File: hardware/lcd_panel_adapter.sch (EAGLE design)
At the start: 50 parts, among them IC1 TPS65131RGET, IC2 LP8867CQPWPRQ1, J1 245863050104829+, J2 54548-2271, U1 TLV62080DSGR

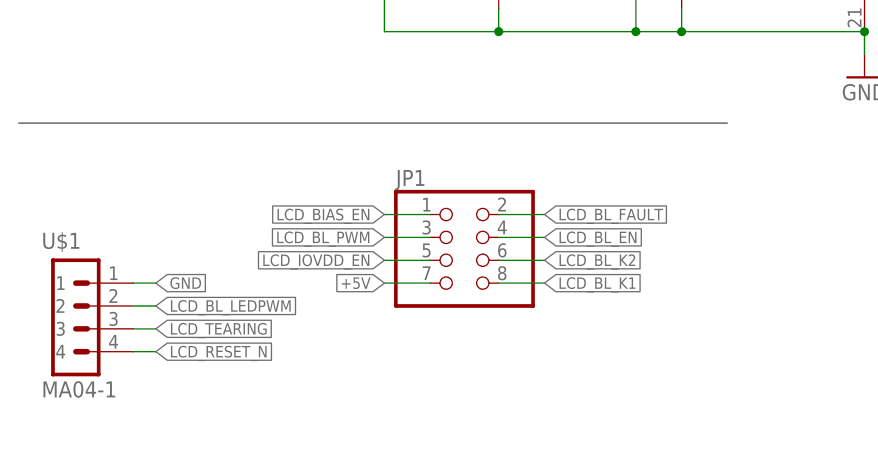
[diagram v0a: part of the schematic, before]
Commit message: added +1.8V pullup resistor for LCD reset pin
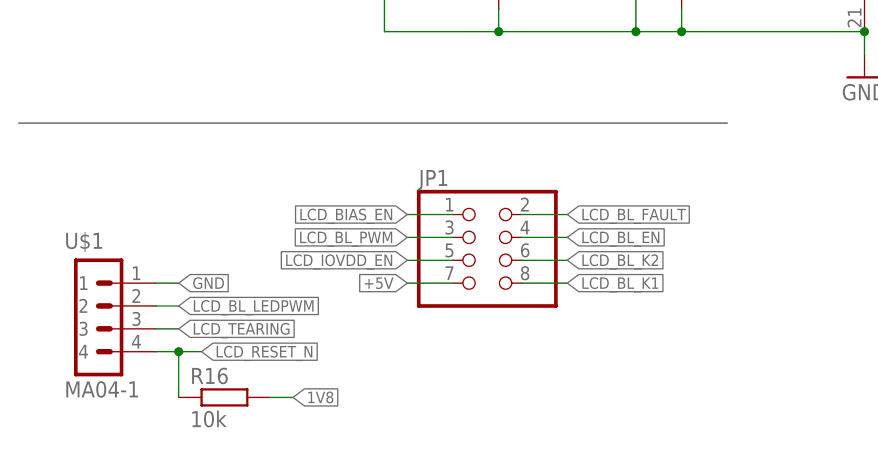
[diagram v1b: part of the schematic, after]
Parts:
- added R16: 10k, rcl:R-EU_R0603
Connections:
- net 1V8: now also R16.2
- net LCD_RESET_N: now also R16.1
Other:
- moved on the sheet: JP1, U$1
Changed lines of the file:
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@@
 <part name="C22" library="rcl" library_urn="urn:adsk.eagle:library:334" deviceset="C-EU" device="C1206" package3d_urn="urn:adsk.eagle:package:23618/2" value="10uF"/>
 <part name="C23" library="rcl" library_urn="urn:adsk.eagle:library:334" deviceset="C-EU" device="C1206" package3d_urn="urn:adsk.eagle:package:23618/2" value="10uF"/>
+<part name="R16" library="rcl" library_urn="urn:adsk.eagle:library:334" deviceset="R-EU_" device="R0603" package3d_urn="urn:adsk.eagle:package:23555/3" value="10k"/>
 </parts>
 <sheets>
@@
 <attribute name="VALUE" x="254" y="50.8" size="1.778" layer="96"/>
 </instance>
-<instance part="U$1" gate="G$1" x="5.08" y="15.24" smashed="yes">
-<attribute name="VALUE" x="2.54" y="5.08" size="1.778" layer="96"/>
-<attribute name="NAME" x="2.54" y="21.59" size="1.778" layer="95"/>
-</instance>
-<instance part="JP1" gate="G$1" x="48.26" y="20.32" smashed="yes">
-<attribute name="NAME" x="41.91" y="28.575" size="1.778" layer="95"/>
-<attribute name="VALUE" x="41.91" y="12.7" size="1.778" layer="96"/>
+<instance part="U$1" gate="G$1" x="7.62" y="15.24" smashed="yes">
+<attribute name="VALUE" x="5.08" y="5.08" size="1.778" layer="96"/>
+<attribute name="NAME" x="5.08" y="21.59" size="1.778" layer="95"/>
+</instance>
+<instance part="JP1" gate="G$1" x="50.8" y="20.32" smashed="yes">
+<attribute name="NAME" x="44.45" y="28.575" size="1.778" layer="95"/>
+<attribute name="VALUE" x="44.45" y="12.7" size="1.778" layer="96"/>
 </instance>
 <instance part="C22" gate="G$1" x="157.48" y="68.58" smashed="yes">
@@
 <attribute name="NAME" x="166.624" y="68.961" size="1.778" layer="95"/>
 <attribute name="VALUE" x="166.624" y="63.881" size="1.778" layer="96"/>
+</instance>
+<instance part="R16" gate="G$1" x="22.86" y="5.08" smashed="yes">
+<attribute name="NAME" x="19.05" y="6.5786" size="1.778" layer="95"/>
+<attribute name="VALUE" x="19.05" y="1.778" size="1.778" layer="96"/>
 </instance>
 </instances>
@@
 <segment>
 <pinref part="U$1" gate="G$1" pin="1"/>
-<wire x1="12.7" y1="17.78" x2="15.24" y2="17.78" width="0.1524" layer="91"/>
-<label x="15.24" y="17.78" size="1.27" layer="95" xref="yes"/>
+<wire x1="15.24" y1="17.78" x2="17.78" y2="17.78" width="0.1524" layer="91"/>
+<label x="17.78" y="17.78" size="1.27" layer="95" xref="yes"/>
 </segment>
 </net>
@@
 </segment>
 <segment>
-<wire x1="45.72" y1="17.78" x2="40.64" y2="17.78" width="0.1524" layer="91"/>
-<label x="40.64" y="17.78" size="1.27" layer="95" rot="R180" xref="yes"/>
+<wire x1="48.26" y1="17.78" x2="43.18" y2="17.78" width="0.1524" layer="91"/>
+<label x="43.18" y="17.78" size="1.27" layer="95" rot="R180" xref="yes"/>
 <pinref part="JP1" gate="G$1" pin="7"/>
 </segment>
@@
 <pinref part="L2" gate="G$1" pin="2"/>
 </segment>
+<segment>
+<pinref part="R16" gate="G$1" pin="2"/>
+<wire x1="27.94" y1="5.08" x2="30.48" y2="5.08" width="0.1524" layer="91"/>
+<label x="30.48" y="5.08" size="1.27" layer="95" xref="yes"/>
+</segment>
 </net>
 <net name="FB" class="0">
@@
 </segment>
 <segment>
-<wire x1="45.72" y1="25.4" x2="40.64" y2="25.4" width="0.1524" layer="91"/>
-<label x="40.64" y="25.4" size="1.27" layer="95" rot="R180" xref="yes"/>
+<wire x1="48.26" y1="25.4" x2="43.18" y2="25.4" width="0.1524" layer="91"/>
+<label x="43.18" y="25.4" size="1.27" layer="95" rot="R180" xref="yes"/>
 <pinref part="JP1" gate="G$1" pin="1"/>
 </segment>
@@
 </segment>
 <segment>
-<wire x1="53.34" y1="17.78" x2="58.42" y2="17.78" width="0.1524" layer="91"/>
-<label x="58.42" y="17.78" size="1.27" layer="95" xref="yes"/>
+<wire x1="55.88" y1="17.78" x2="60.96" y2="17.78" width="0.1524" layer="91"/>
+<label x="60.96" y="17.78" size="1.27" layer="95" xref="yes"/>
 <pinref part="JP1" gate="G$1" pin="8"/>
 </segment>
@@
 </segment>
 <segment>
-<wire x1="53.34" y1="20.32" x2="58.42" y2="20.32" width="0.1524" layer="91"/>
-<label x="58.42" y="20.32" size="1.27" layer="95" xref="yes"/>
+<wire x1="55.88" y1="20.32" x2="60.96" y2="20.32" width="0.1524" layer="91"/>
+<label x="60.96" y="20.32" size="1.27" layer="95" xref="yes"/>
 <pinref part="JP1" gate="G$1" pin="6"/>
 </segment>
@@
 </segment>
 <segment>
-<wire x1="53.34" y1="22.86" x2="58.42" y2="22.86" width="0.1524" layer="91"/>
-<label x="58.42" y="22.86" size="1.27" layer="95" xref="yes"/>
+<wire x1="55.88" y1="22.86" x2="60.96" y2="22.86" width="0.1524" layer="91"/>
+<label x="60.96" y="22.86" size="1.27" layer="95" xref="yes"/>
 <pinref part="JP1" gate="G$1" pin="4"/>
 </segment>
@@
 </segment>
 <segment>
-<wire x1="53.34" y1="25.4" x2="58.42" y2="25.4" width="0.1524" layer="91"/>
-<label x="58.42" y="25.4" size="1.27" layer="95" xref="yes"/>
+<wire x1="55.88" y1="25.4" x2="60.96" y2="25.4" width="0.1524" layer="91"/>
+<label x="60.96" y="25.4" size="1.27" layer="95" xref="yes"/>
 <pinref part="JP1" gate="G$1" pin="2"/>
 </segment>
@@
 </segment>
 <segment>
-<wire x1="45.72" y1="22.86" x2="40.64" y2="22.86" width="0.1524" layer="91"/>
-<label x="40.64" y="22.86" size="1.27" layer="95" rot="R180" xref="yes"/>
+<wire x1="48.26" y1="22.86" x2="43.18" y2="22.86" width="0.1524" layer="91"/>
+<label x="43.18" y="22.86" size="1.27" layer="95" rot="R180" xref="yes"/>
 <pinref part="JP1" gate="G$1" pin="3"/>
 </segment>
@@
 </segment>
 <segment>
-<wire x1="15.24" y1="10.16" x2="12.7" y2="10.16" width="0.1524" layer="91"/>
-<label x="15.24" y="10.16" size="1.27" layer="95" xref="yes"/>
+<wire x1="17.78" y1="10.16" x2="15.24" y2="10.16" width="0.1524" layer="91"/>
+<label x="20.32" y="10.16" size="1.27" layer="95" xref="yes"/>
 <pinref part="U$1" gate="G$1" pin="4"/>
+<pinref part="R16" gate="G$1" pin="1"/>
+<wire x1="17.78" y1="10.16" x2="17.78" y2="5.08" width="0.1524" layer="91"/>
+<wire x1="17.78" y1="10.16" x2="20.32" y2="10.16" width="0.1524" layer="91"/>
+<junction x="17.78" y="10.16"/>
 </segment>
 </net>
@@
 <segment>
 <pinref part="U$1" gate="G$1" pin="2"/>
-<wire x1="12.7" y1="15.24" x2="15.24" y2="15.24" width="0.1524" layer="91"/>
-<label x="15.24" y="15.24" size="1.27" layer="95" xref="yes"/>
+<wire x1="15.24" y1="15.24" x2="17.78" y2="15.24" width="0.1524" layer="91"/>
+<label x="17.78" y="15.24" size="1.27" layer="95" xref="yes"/>
 </segment>
 </net>
@@
 <segment>
 <pinref part="U$1" gate="G$1" pin="3"/>
-<wire x1="12.7" y1="12.7" x2="15.24" y2="12.7" width="0.1524" layer="91"/>
-<label x="15.24" y="12.7" size="1.27" layer="95" xref="yes"/>
+<wire x1="15.24" y1="12.7" x2="17.78" y2="12.7" width="0.1524" layer="91"/>
+<label x="17.78" y="12.7" size="1.27" layer="95" xref="yes"/>
 </segment>
 </net>
 <net name="LCD_IOVDD_EN" class="0">
 <segment>
-<wire x1="45.72" y1="20.32" x2="40.64" y2="20.32" width="0.1524" layer="91"/>
-<label x="40.64" y="20.32" size="1.27" layer="95" rot="R180" xref="yes"/>
+<wire x1="48.26" y1="20.32" x2="43.18" y2="20.32" width="0.1524" layer="91"/>
+<label x="43.18" y="20.32" size="1.27" layer="95" rot="R180" xref="yes"/>
 <pinref part="JP1" gate="G$1" pin="5"/>
 </segment>

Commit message: updated the backlight driver IC from LP8867 to TPS61194
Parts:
- removed IC2: LP8867CQPWPRQ1, SamacSys_Parts:LP8867CQPWPRQ1
- added IC3: TPS61194PWPR, SamacSys_Parts:TPS61194PWPR
- C12: value 12pF -> 75pF
- C8: value 15pF -> 12pF
- R13: value 60k -> 62k
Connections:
- net +5V: now also IC3.VIN_1, IC3.VIN_2; no longer IC2.VIN_1, IC2.VIN_2
- net GND: now also IC3.EP, IC3.GND_1, IC3.GND_2, IC3.OUT3, IC3.OUT4, IC3.PGND; no longer IC2.EP, IC2.GND_1, IC2.GND_2, IC2.OUT3, IC2.OUT4, IC2.PGND
- net LCD_BL_EN: now also IC3.SYNC, IC3.VDDIO/EN; no longer IC2.SYNC, IC2.VDDIO/EN
- net LCD_BL_FAULT: now also IC3.FAULT; no longer IC2.FAULT
- net LCD_BL_K1: now also IC3.OUT1; no longer IC2.OUT1
- net LCD_BL_K2: now also IC3.OUT2; no longer IC2.OUT2
- net LCD_BL_PWM: now also IC3.PWM; no longer IC2.PWM
- net N$14: now also IC3.FB; no longer IC2.FB
- net N$15: now also IC3.LDO; no longer IC2.LDO
- net N$16: now also IC3.ISET; no longer IC2.ISET
- net N$17: now also IC3.FSET; no longer IC2.FSET
- net N$3: now also IC3.SW; no longer IC2.SW

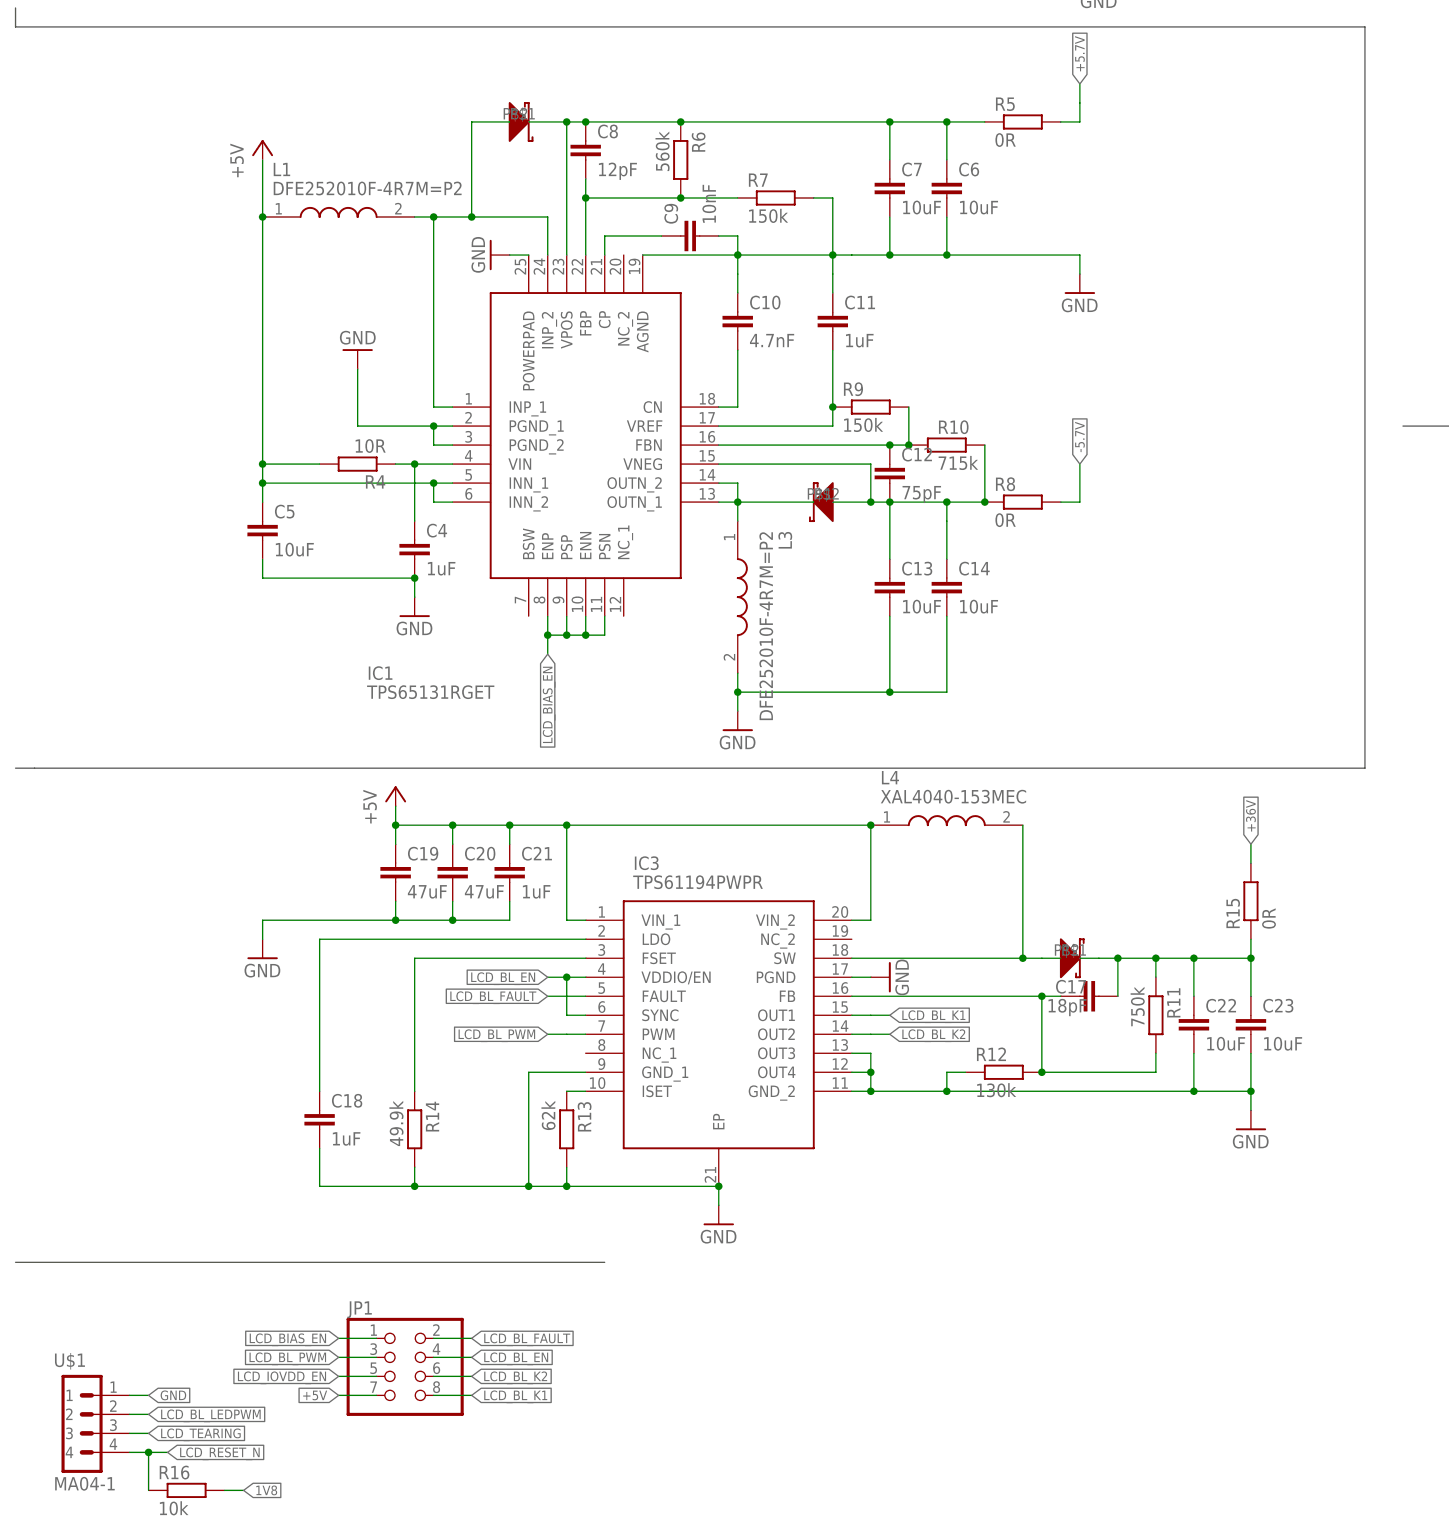
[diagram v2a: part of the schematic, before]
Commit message: revert back from TPS61194 to LP8867, and add transistors
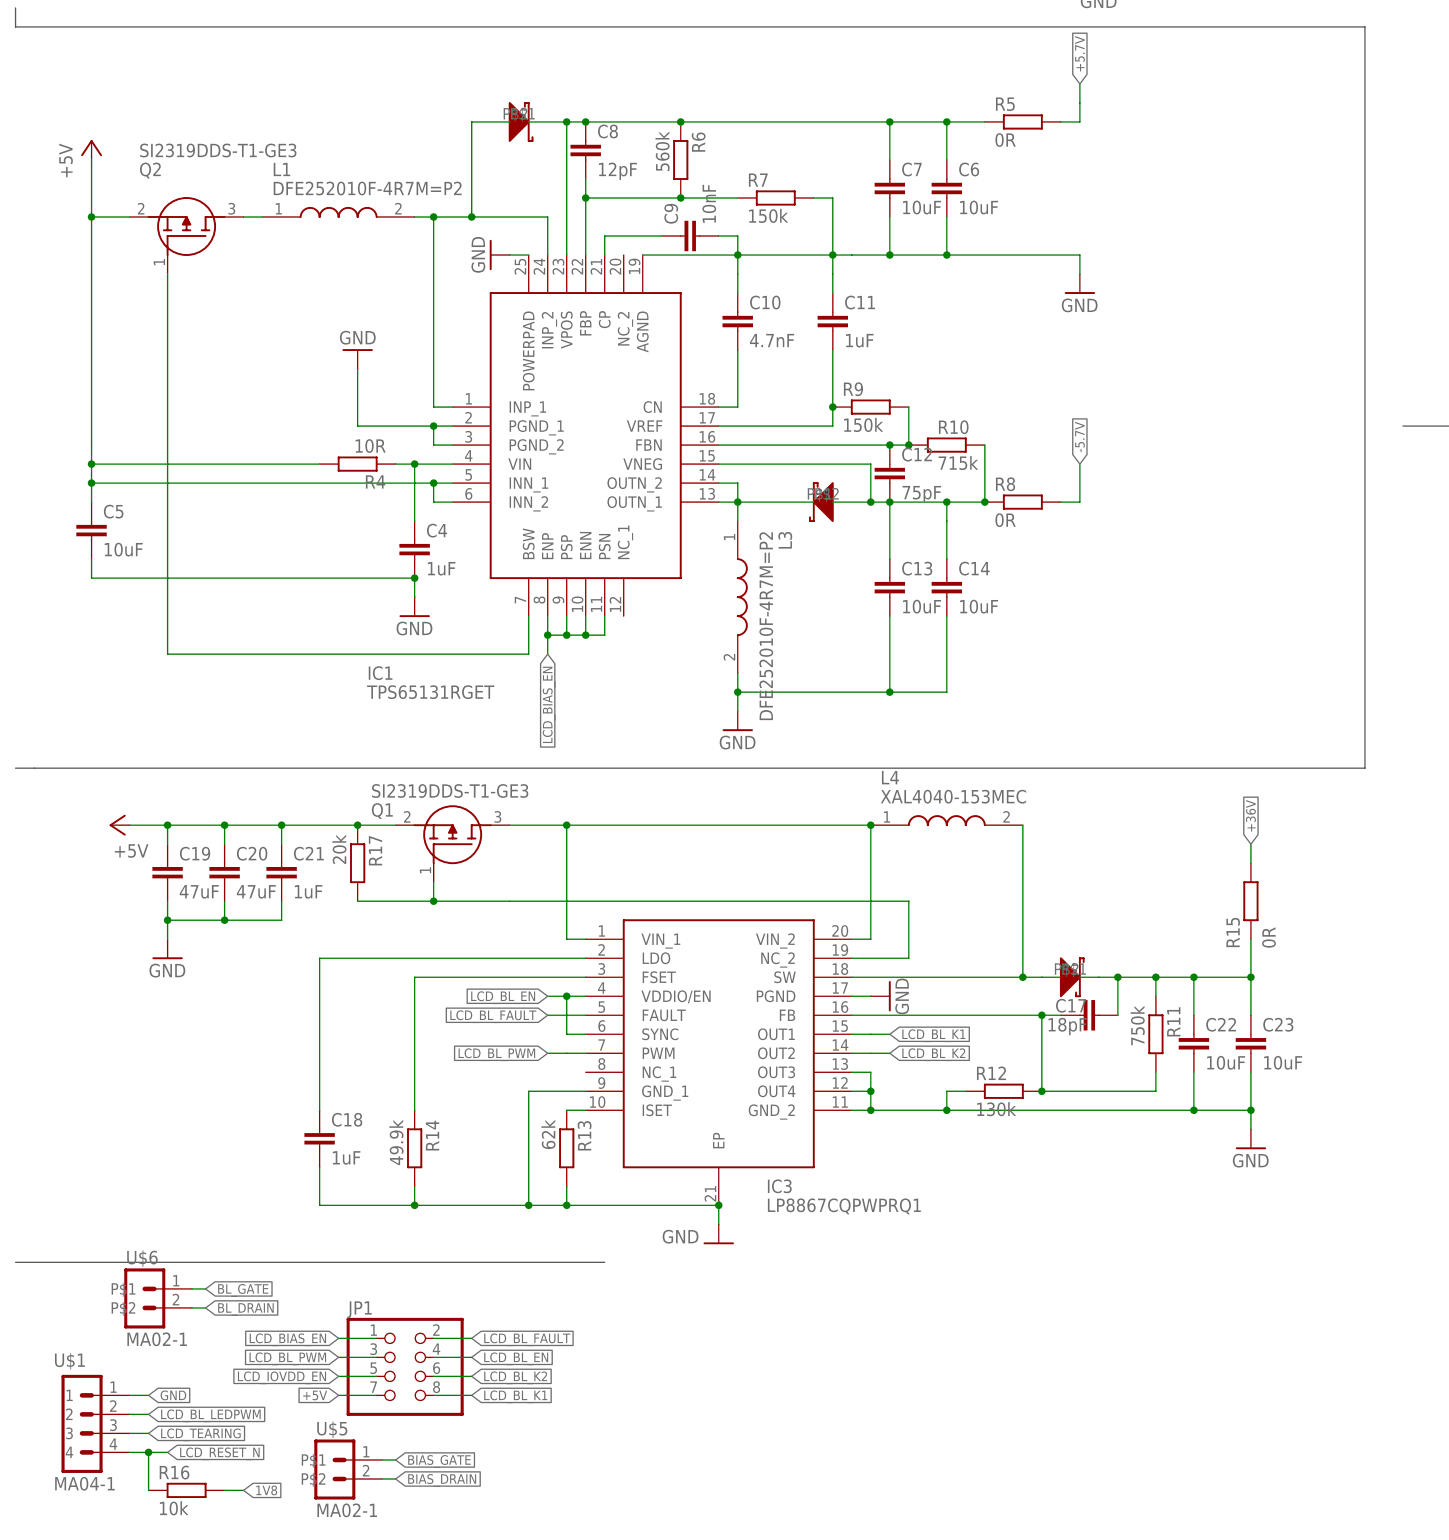
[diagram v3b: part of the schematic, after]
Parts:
- added Q1, Q2: SI2319DDS-T1-GE3, SamacSys_Parts:SI2319DDS-T1-GE3
- added R17: 20k, rcl:R-EU_R0603
- added U$5, U$6: MA02-1, custom_library:MA02-1
- IC3: value TPS61194PWPR -> LP8867CQPWPRQ1
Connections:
- new net BIAS_DRAIN: L1.1, Q2.D, U$5.P$2
- new net BIAS_GATE: IC1.BSW, Q2.G, U$5.P$1
- new net BL_DRAIN: IC3.VIN_1, IC3.VIN_2, L4.1, Q1.D, U$6.P$2
- new net BL_GATE: IC3.NC_2, Q1.G, R17.2, U$6.P$1
- net +5V: now also Q1.S, Q2.S, R17.1; no longer IC3.VIN_1, IC3.VIN_2, L1.1, L4.1
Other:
- moved on the sheet: C17, C18, C19, C20, C21, C22, C23, C5, IC3, R11, R12, R13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
